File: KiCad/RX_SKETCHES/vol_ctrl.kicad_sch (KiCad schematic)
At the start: 6 parts

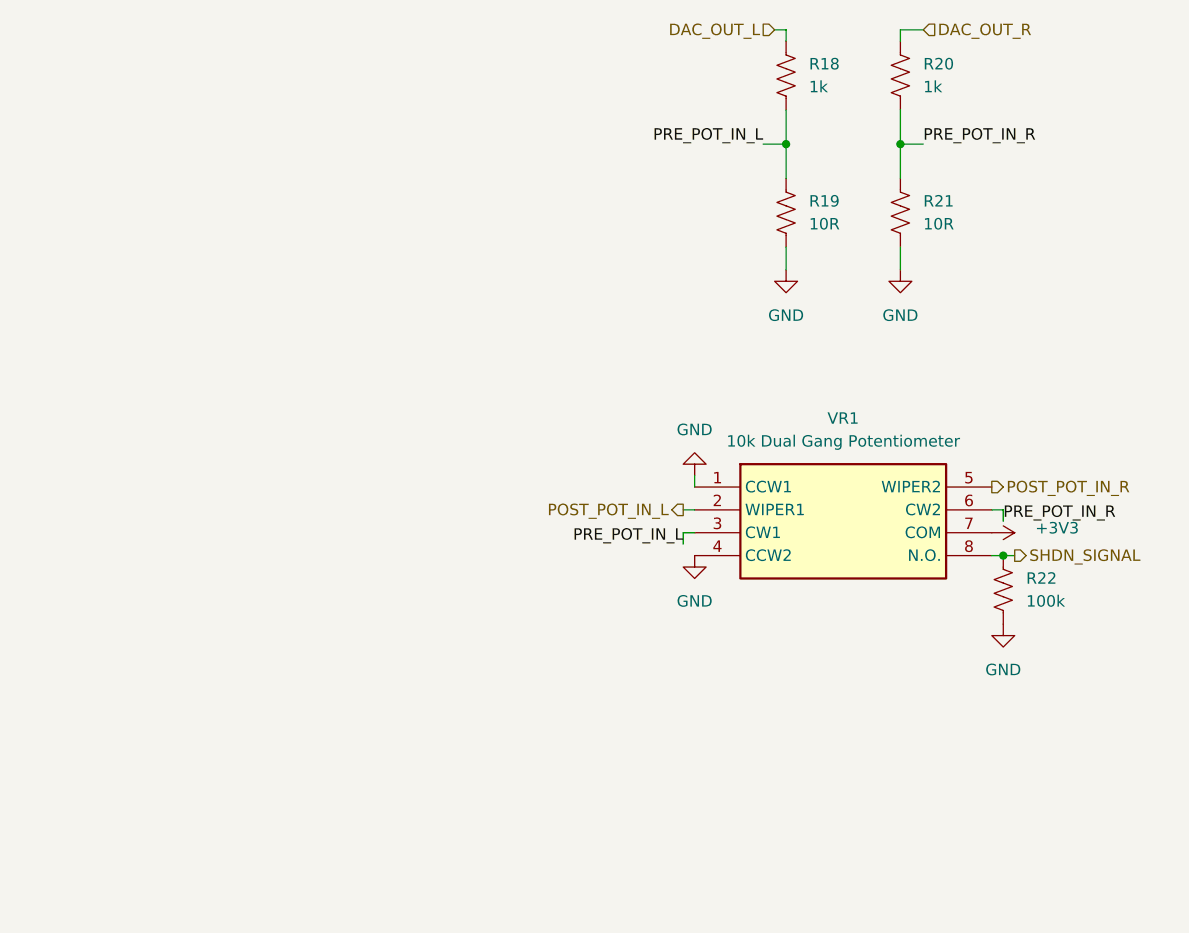
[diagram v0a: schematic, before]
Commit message: RX v1: complete PCB layout, retune analog chain, fix ESD clamp placement
Brings the RX schematic and board up to a fabricable state. DRC is clean:
zero unconnected items, zero schematic-parity issues. The 16 remaining
violations are footprint-inherent and documented rather than worked around
(ESP32-WROOM thermal via array drilled 0.2 mm against a 0.3 mm rule, and
USB-C NPTH-to-pad spacing from the vendor land pattern).

Analog:
- Gain network populated at RF 4.7k / RIN 47k (-20 dB) rather than DNP 10k.
  Tames the PCM5102's 2.1 Vrms into sensitive IEMs, gives the 10k pot a
  4.7x loading ratio instead of 1:1, and lifts the coupling corner clear of
  the audible band.
- Coupling caps C1-C4 raised 0.47uF -> 1uF. Corner 7.2 Hz -> 3.4 Hz, and it
  halves the signal developed across the ceramic at 20 Hz, which is where
  Class-II dielectric distortion actually shows up.
- PCM5102 mode pins no longer float: 100k pulldowns on FLT and XSMT, with
  DEMP and FMT strapped to GND.

Power and protection:
- D1's third TVS channel moved off the switched +5V rail onto VBUS_RAW. An
  ESD clamp has to sit on the connector pin exposed to a finger; behind the
  power switch it disconnected exactly when the board is most likely to be
  handled. The off state is unaffected -- a TVS is open below its standoff
  voltage and SW4 still breaks the rail.
- All three slide switches now follow one rule: the open throw is the safe
  default (powered off / normal-latency filter / muted).

Housekeeping:
- C28 and mounting holes REF1-REF4 added to the schematic, clearing parity
  errors against parts that previously existed only on the PCB.
- Gain, loudness, and filter math written up in README.org with sources so
  the numbers can be re-derived; rationale logged in hardware_revisions.org.
- .gitignore now covers the editor .history/ directory and ESP-IDF build
  output, which were showing up as untracked noise.

Firmware and build artifacts are deliberately excluded from this commit.

Co-authored-b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
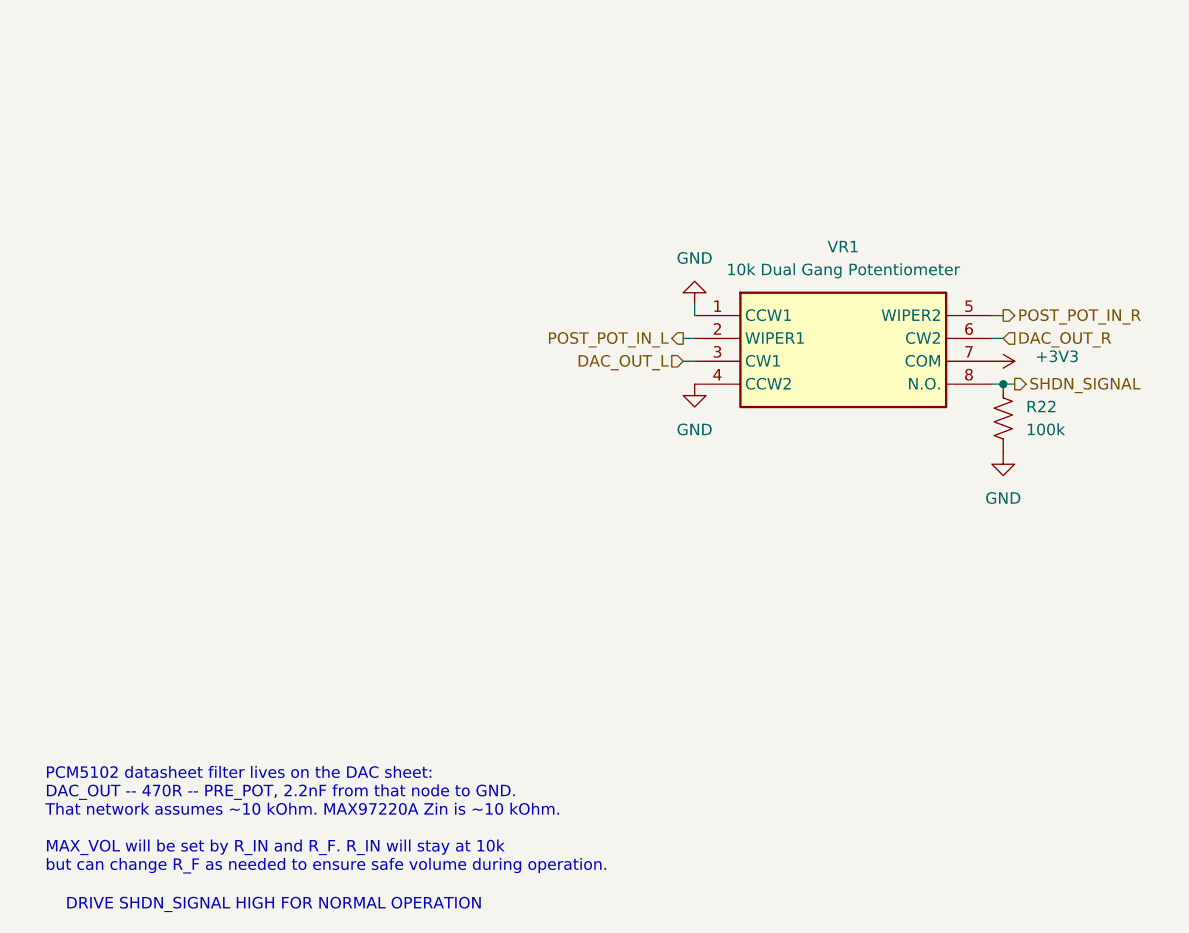
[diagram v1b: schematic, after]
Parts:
- removed R18, R20: 1k, Resistor_SMD:R_0201_0603Metric, symbol Device:R_US
- removed R19, R21: 10R, Resistor_SMD:R_0201_0603Metric, symbol Device:R_US
- R22: footprint Resistor_SMD:R_0201_0603Metric -> Resistor_SMD:R_0805_2012Metric_Pad1.20x1.40mm_HandSolder
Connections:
- net PRE_POT_IN_L is gone; now on net DAC_OUT_L: VR1.3 (CW1)
- net PRE_POT_IN_R is gone; now on net DAC_OUT_R: VR1.6 (CW2)
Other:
- note added: "DRIVE SHDN_SIGNAL HIGH FOR NORMAL OPERATION"
- note added: "PCM5102 datasheet filter lives on the DAC sheet: DAC_OUT -- 470R -- PRE_POT, 2.2nF from that node to GND. That network assumes ~10 kOhm. MAX97220A Zin is ~10 kOhm. MAX_VOL will be set by R_IN and R_F. R_IN will stay at 10k but can change R_F as needed to ensure safe volume during operation."
- moved on the sheet: R22, VR1
